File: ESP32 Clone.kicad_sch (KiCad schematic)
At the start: 34 parts, among them J1 USB_C_Plug_USB2.0, J2 Conn_01x19_Male, J3 Conn_01x19_Male, Q1 MMSS8050-H-TP, Q2 MMSS8050-H-TP, SW1 SW_Push, SW2 SW_Push, U1 CP2102N-A01-GQFN28, U2 AMS1117

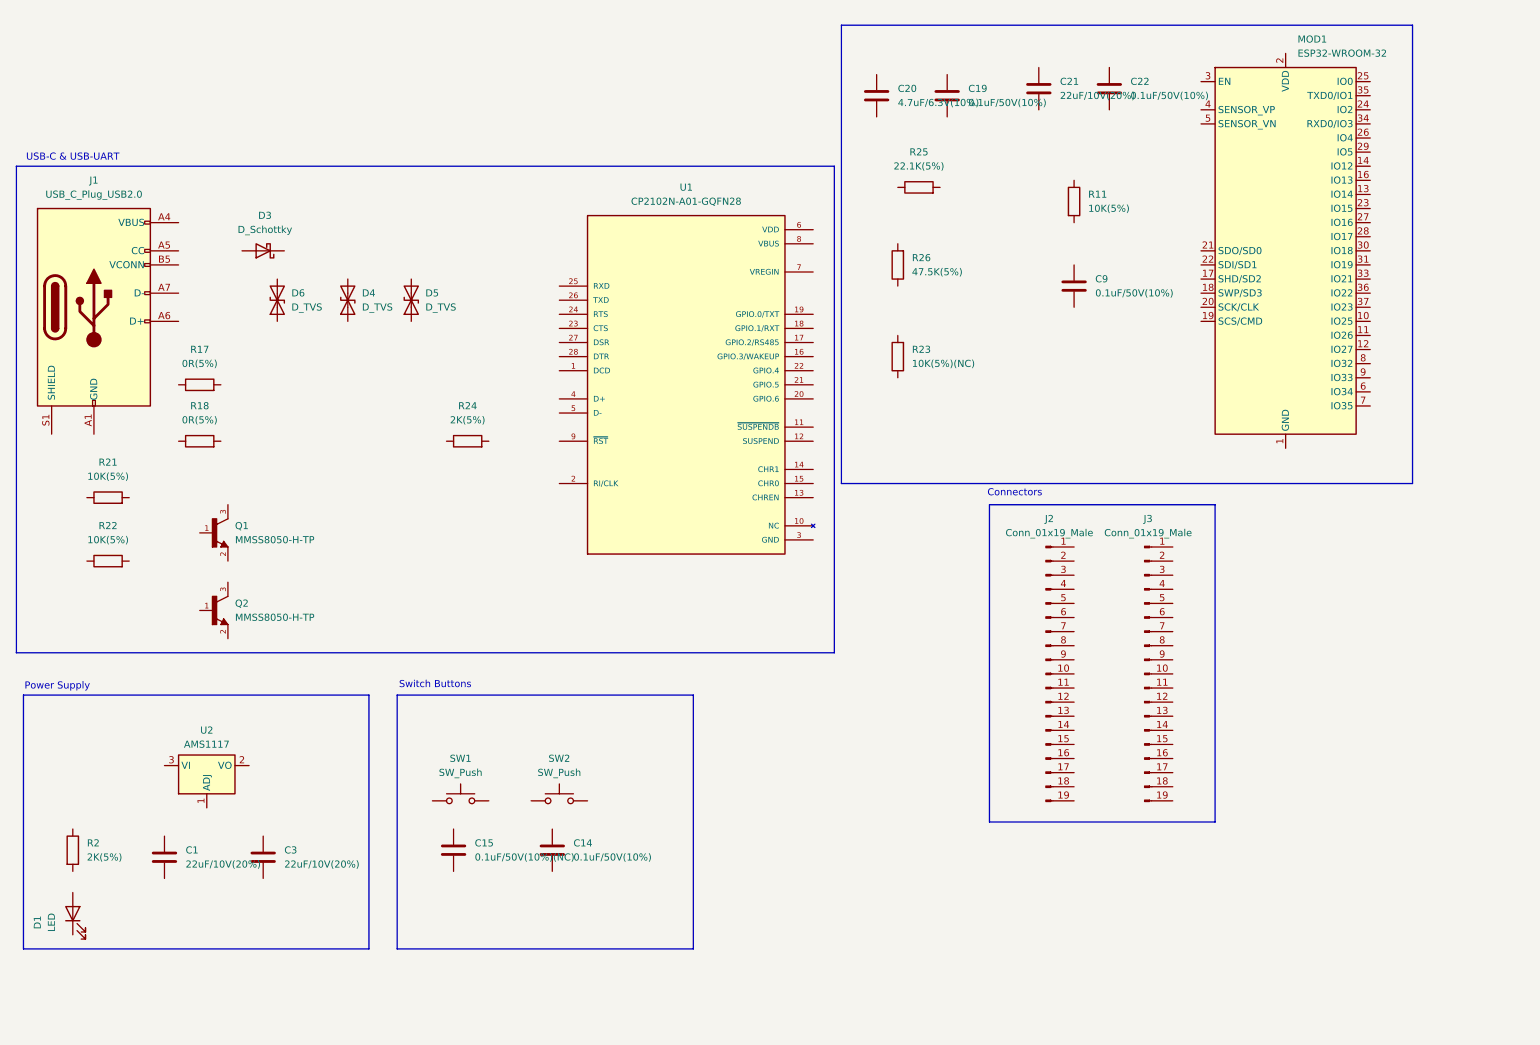
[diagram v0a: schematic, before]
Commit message: Paar Net labels en draden gemaakt
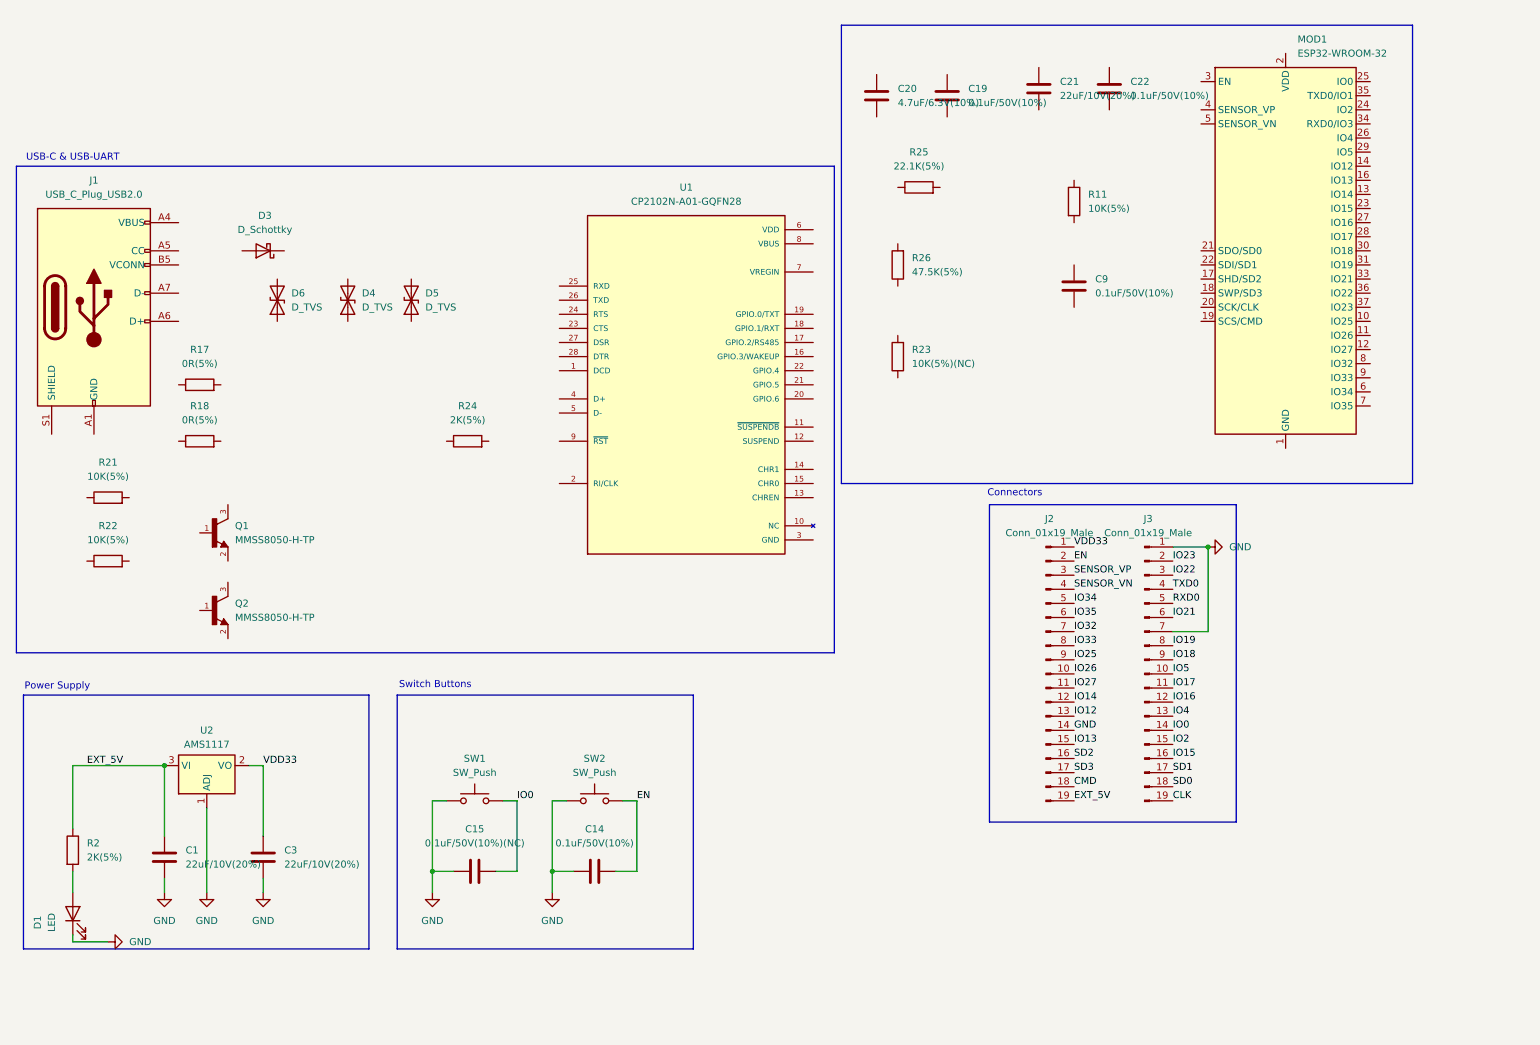
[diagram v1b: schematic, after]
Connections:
- net GND: now also C1.2, C14.1, C15.2, C3.2, D1.1 (K), J2.14 (Pin_14), J3.1 (Pin_1), J3.7 (Pin_7), SW1.1, SW2.1, U2.1 (ADJ)
- net EXT_5V: now reaches R2.1
- net EXT_5V: now also C1.1, J2.19 (Pin_19), U2.3 (VI)
- net at R2.2: now also D1.2 (A)
- net VDD33: now reaches C3.1
- net VDD33: now also J2.1 (Pin_1), U2.2 (VO)
- net EN: now reaches C14.2
- net EN: now also J2.2 (Pin_2), SW2.2
- net IO0: now reaches SW1.2
- net IO0: now also C15.1, J3.14 (Pin_14)
- net IO26: now reaches J2.10 (Pin_10)
- net IO27: now reaches J2.11 (Pin_11)
- net IO14: now reaches J2.12 (Pin_12)
- net IO12: now reaches J2.13 (Pin_13)
- net IO13: now reaches J2.15 (Pin_15)
- net SD2: now reaches J2.16 (Pin_16)
- net SD3: now reaches J2.17 (Pin_17)
- net CMD: now reaches J2.18 (Pin_18)
- net SENSOR_VP: now reaches J2.3 (Pin_3)
- net SENSOR_VN: now reaches J2.4 (Pin_4)
- net IO34: now reaches J2.5 (Pin_5)
- net IO35: now reaches J2.6 (Pin_6)
- net IO32: now reaches J2.7 (Pin_7)
- net IO33: now reaches J2.8 (Pin_8)
- net IO25: now reaches J2.9 (Pin_9)
- net IO5: now reaches J3.10 (Pin_10)
- net IO17: now reaches J3.11 (Pin_11)
- net IO16: now reaches J3.12 (Pin_12)
- net IO4: now reaches J3.13 (Pin_13)
- net IO2: now reaches J3.15 (Pin_15)
- net IO15: now reaches J3.16 (Pin_16)
- net SD1: now reaches J3.17 (Pin_17)
- net SD0: now reaches J3.18 (Pin_18)
- net CLK: now reaches J3.19 (Pin_19)
- net IO23: now reaches J3.2 (Pin_2)
- net IO22: now reaches J3.3 (Pin_3)
- net TXD0: now reaches J3.4 (Pin_4)
- net RXD0: now reaches J3.5 (Pin_5)
- net IO21: now reaches J3.6 (Pin_6)
- net IO19: now reaches J3.8 (Pin_8)
- net IO18: now reaches J3.9 (Pin_9)
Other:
- moved on the sheet: C14, C15, SW1, SW2

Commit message: SCHEMA KLAAR
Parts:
- added C2: 100nF, Capacitor_SMD:C_0402_1005Metric, symbol Device:C
- added C4: 0.1uF, Capacitor_SMD:C_0402_1005Metric, symbol Device:C
- added H1, H2, H3, H4: MountingHole, MountingHole:MountingHole_2.1mm, symbol Mechanical:MountingHole
- added R1, R3: 4,7K, Resistor_SMD:R_0402_1005Metric, symbol Device:R
- added R4: 4.7K, Resistor_SMD:R_0402_1005Metric, symbol Device:R
- added U3: AHT20, AHT20:PSON100P300X300X110-6N, symbol AHT20:AHT20
- added U4: BH1750FVI-TR, BH1750FVI-TR:XDCR_BH1750FVI-TR, symbol BH1750:BH1750FVI-TR
- added U5: 24LC1025-I/P, PDIP8_300MC_MCH, symbol 24LC1025-I_SN:24LC1025-I_P
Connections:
- net RXD0 is gone; now on net IO3: J3.5 (Pin_5)
- net TXD0 is gone; now on net IO1: J3.4 (Pin_4)
- net CLK: now also MOD1.20 (SCK/CLK)
- net CMD: now also MOD1.19 (SCS/CMD)
- net EN: now also C9.1, MOD1.3 (EN), Q1.3, R11.2
- net EXT_5V: now also D3.1 (K)
- net GND: now also C19.2, C20.2, C21.2, C22.2, C9.2, D4.1 (A1), D5.1 (A1), D6.1 (A1), J1.A1 (GND), J1.A12 (GND), J1.B1 (GND), J1.B12 (GND), J1.S1 (SHIELD), MOD1.1 (GND), MOD1.15 (GND), MOD1.38 (GND), MOD1.39 (GND), R23.1, R26.1, C2.2, C4.1, U3.5 (GND), U4.3 (GND), U5.2 (A1), U5.4 (VSS), U5.7 (WP)
- net IO0: now also MOD1.25 (IO0), Q2.2
- net IO12: now also MOD1.14 (IO12)
- net IO13: now also MOD1.16 (IO13)
- net IO14: now also MOD1.13 (IO14)
- net IO15: now also MOD1.23 (IO15)
- net IO18: now also MOD1.30 (IO18)
- net IO19: now also MOD1.31 (IO19)
- net IO2: now also MOD1.24 (IO2)
- net IO21: now also MOD1.33 (IO21)
- net IO22: now also MOD1.36 (IO22)
- net IO23: now also MOD1.37 (IO23)
- net IO25: now also MOD1.10 (IO25)
- net IO26: now also MOD1.11 (IO26)
- net IO27: now also MOD1.12 (IO27)
- net IO32: now also MOD1.8 (IO32)
- net IO33: now also MOD1.9 (IO33)
- net IO34: now also MOD1.6 (IO34)
- net IO35: now also MOD1.7 (IO35)
- net IO4: now also MOD1.26 (IO4)
- net IO5: now also MOD1.29 (IO5)
- net SD0: now also MOD1.21 (SDO/SD0)
- net SD1: now also MOD1.22 (SDI/SD1)
- net SD2: now also MOD1.17 (SHD/SD2)
- net SD3: now also MOD1.18 (SWP/SD3)
- net SENSOR_VN: now also MOD1.5 (SENSOR_VN)
- net SENSOR_VP: now also MOD1.4 (SENSOR_VP)
- net VDD33: now also C19.1, C20.1, C21.1, C22.1, MOD1.2 (VDD), R11.1, R24.1, U1.6 (VDD), U1.7 (VREGIN), C2.1, R1.2, R3.2, R4.1, U3.2 (VDD), U4.1 (VCC), U5.1 (A0), U5.3 (A2), U5.8 (VCC)
- net RTS: now reaches R22.1
- net RTS: now also Q1.2, U1.24 (RTS)
- net at R22.2: now also Q2.1
- net USB_DP: now reaches D5.2 (A2)
- net USB_DP: now also J1.A6 (D+), U1.4 (D+)
- net VBUS: now reaches D3.2 (A)
- net VBUS: now also D6.2 (A2), J1.A4 (VBUS), J1.A9 (VBUS), J1.B4 (VBUS), J1.B9 (VBUS), R25.2
- net at Q1.1: now also R21.2
- net IO3: now reaches R18.1
- net IO3: now also MOD1.34 (RXD0/IO3)
- net TXD: now reaches R18.2
- net TXD: now also U1.26 (TXD)
- net at U1.11 (~{SUSPENDB}): now also R23.2
- net RXD: now reaches U1.25 (RXD)
- net RXD: now also R17.2
- net DTR: now reaches U1.28 (DTR)
- net DTR: now also Q2.3, R21.1
- net USB_DN: now reaches U1.5 (D-)
- net USB_DN: now also D4.2 (A2), J1.A7 (D-)
- net at U1.8 (VBUS): now also R25.1, R26.2
- net at U1.9 (~{RST}): now also R24.2
- net IO1: now reaches R17.1
- net IO1: now also MOD1.35 (TXD0/IO1)
- net SDA: now reaches MOD1.27 (IO16)
- net SDA: now also R3.1, U3.4 (SDA), U4.4 (SDA), U5.5 (SDA)
- net SCL: now reaches MOD1.28 (IO17)
- net SCL: now also R1.1, U3.3 (SCL), U4.6 (SCL), U5.6 (SCL)
- net IO16: no longer names the net of J3.12 (Pin_12)
- net IO17: no longer names the net of J3.11 (Pin_11)
- new net: C4.2, R4.2, U4.5 (DVI)
- new net: U3.1 (NC), U3.6 (NC)
- no-connect marks 0 -> 20
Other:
- note added: "EEProm"
- note added: "ESP32 Module"
- note added: "Lightintensity sensor"
- note added: "Pull-Up SCL + SDA"
- note added: "Relative Humidity Sensor"
- moved on the sheet: C1, C14, C15, C19, C20, C21, C22, C3, C9, D1, D3, D4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
